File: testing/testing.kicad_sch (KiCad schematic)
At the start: 3 parts

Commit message: Testing Commit 12
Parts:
- added D4, D5, D6: LED, symbol Device:LED
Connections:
- net +BATT: now also D4.2 (A), D5.2 (A), D6.2 (A)
- net GND: now also D4.1 (K), D5.1 (K), D6.1 (K)

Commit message: Test Commit 13
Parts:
- removed D4, D5, D6: LED, symbol Device:LED

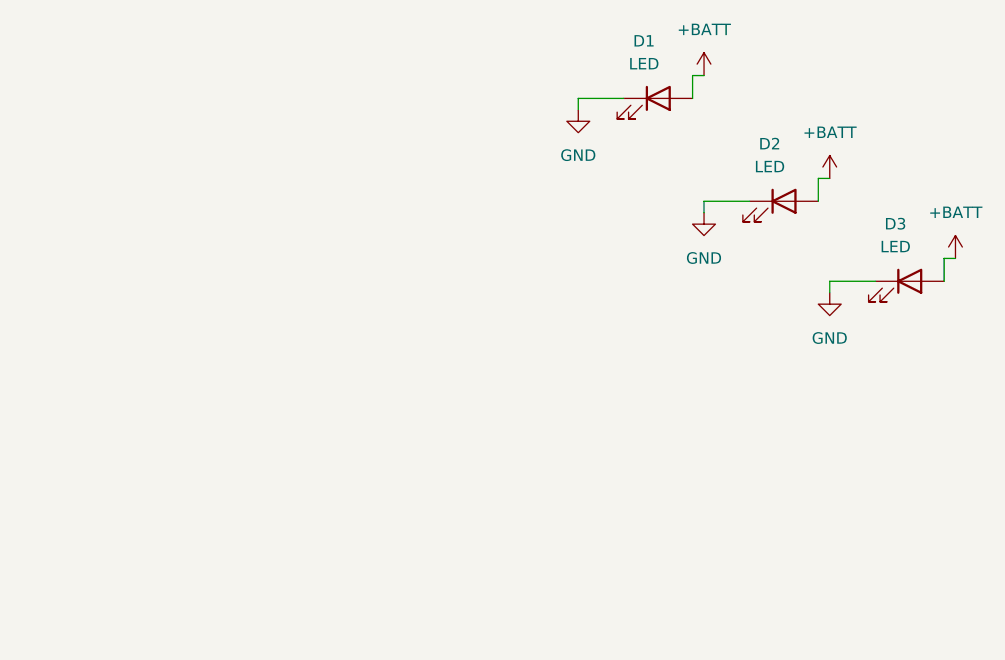
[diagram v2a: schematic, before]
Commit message: Test Commit 10 + Removed test.yml
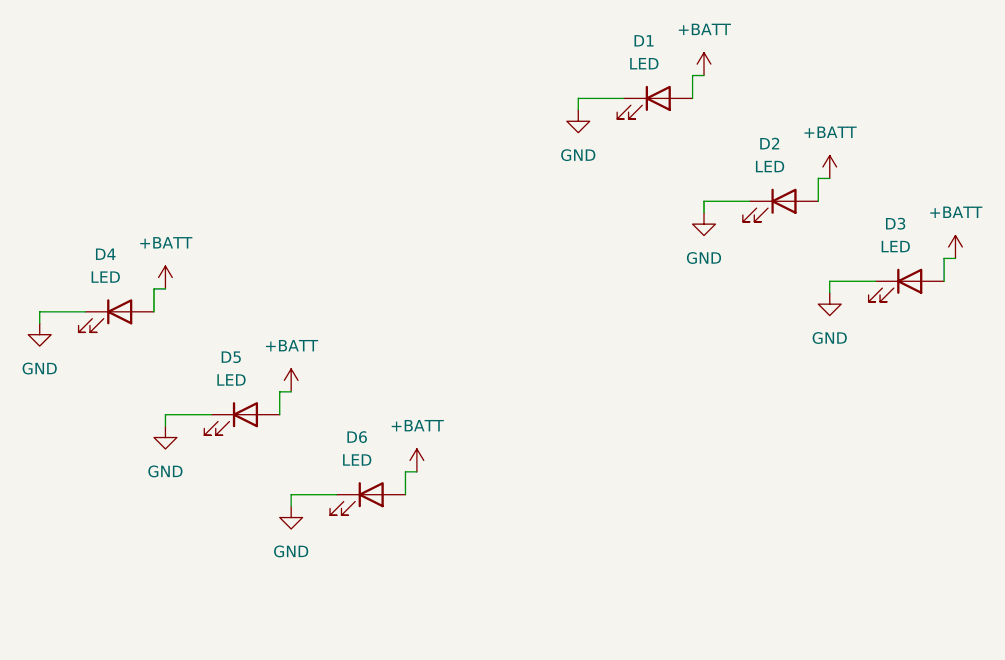
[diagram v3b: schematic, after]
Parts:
- added D4, D5, D6: LED, symbol Device:LED
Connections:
- net +BATT: now also D4.2 (A), D5.2 (A), D6.2 (A)
- net GND: now also D4.1 (K), D5.1 (K), D6.1 (K)

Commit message: Test Commit 11
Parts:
- removed D4, D5, D6: LED, symbol Device:LED
